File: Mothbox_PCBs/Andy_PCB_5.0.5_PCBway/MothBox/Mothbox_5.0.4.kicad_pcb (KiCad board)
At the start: 2 copper layers, 237 x 139 mm, 182 parts, among them J1 DB141V-2.54-4P, J2 DB141V-2.54-4P, J3 DB141V-2.54-4P, J4 DB141V-2.54-4P, J5 Conn_1.25mm, Q1 AP30P30Q, Q10 AP30P30Q, Q13 AP30P30Q, Q2 AO3400A, Q3 YJQ10N2A, Q4 YJQ10N2A, Q5 YJQ10N2A, Q6 YJQ10N2A, Q7 YJQ10N2A, Q8 AP30P30Q, Q9 YJQ10N2A, SW2 KH-6X6X5H-STM, U10 Days, U11 Hours3, U12 MODE, U13 Hours1, U14 Hours2, U15 PCA9555PW, U16 PCA9555PW, U17 DS18B20U, U18 LTR-303ALS-01, U19 graphic, U2 XL4015E1, U3 INA219BIDCNT, U5 RASPBERRY_PI_5, U6 RASPBERRY_PI_4B_4GB, U7 Female Inv Socket Pi 2.54-2*20, U8 GPs 5 pin PM2.54-1*5, U9 PCA9555PW

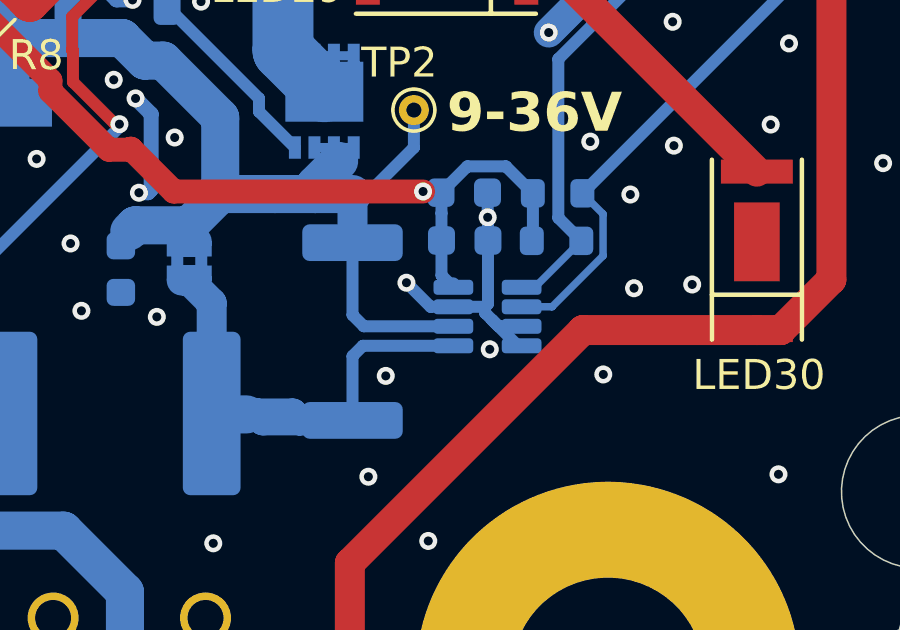
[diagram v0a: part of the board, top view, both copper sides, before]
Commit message: new IC for 219 with smaller pads , ignoring zip files
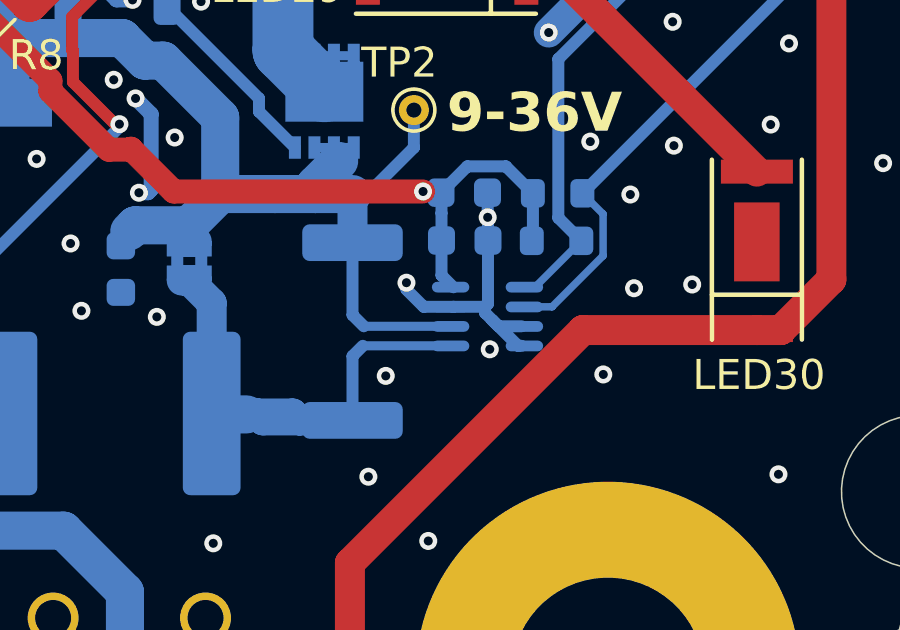
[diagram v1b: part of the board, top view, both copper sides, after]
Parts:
- U3: footprint MothBox_footprints_Library:SOT-23-8 -> easyeda2kicad:SOT-23-8_L3.0-W1.7-P0.65-LS2.8-BR
- turned U3 to 180 degrees

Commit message: tweaked incorrect descriptions for some parts
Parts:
- R32: value 100R -> 0R
- SW2: value KH-6X6X5H-STM -> 4-1437565-1
- U3: value INA219BIDCNT -> TI INA219AIDCNR
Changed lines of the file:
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@@
 			)
 		)
-		(property "Value" "INA219BIDCNT"
+		(property "Value" "TI INA219AIDCNR"
 			(at 0 -4.98 0)
 			(layer "B.Fab")
@@
 			)
 		)
-		(property "Value" "KH-6X6X5H-STM"
+		(property "Value" "4-1437565-1"
 			(at 0 -6.25 0)
 			(layer "B.Fab")
@@
 			)
 		)
-		(property "Description" ""
+		(property "Description" "   Tactile Switch SPST 160gf 4.98mm Gull Wing 6mm x 6mm Surface Mount"
 			(at 0 0 0)
 			(layer "B.Fab")
@@
 			)
 		)
-		(property "Value" "100R"
+		(property "Value" "0R"
 			(at 0 -1.43 0)
 			(layer "B.Fab")
